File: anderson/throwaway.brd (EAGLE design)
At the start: 37.8 x 29.2 mm, 4 parts

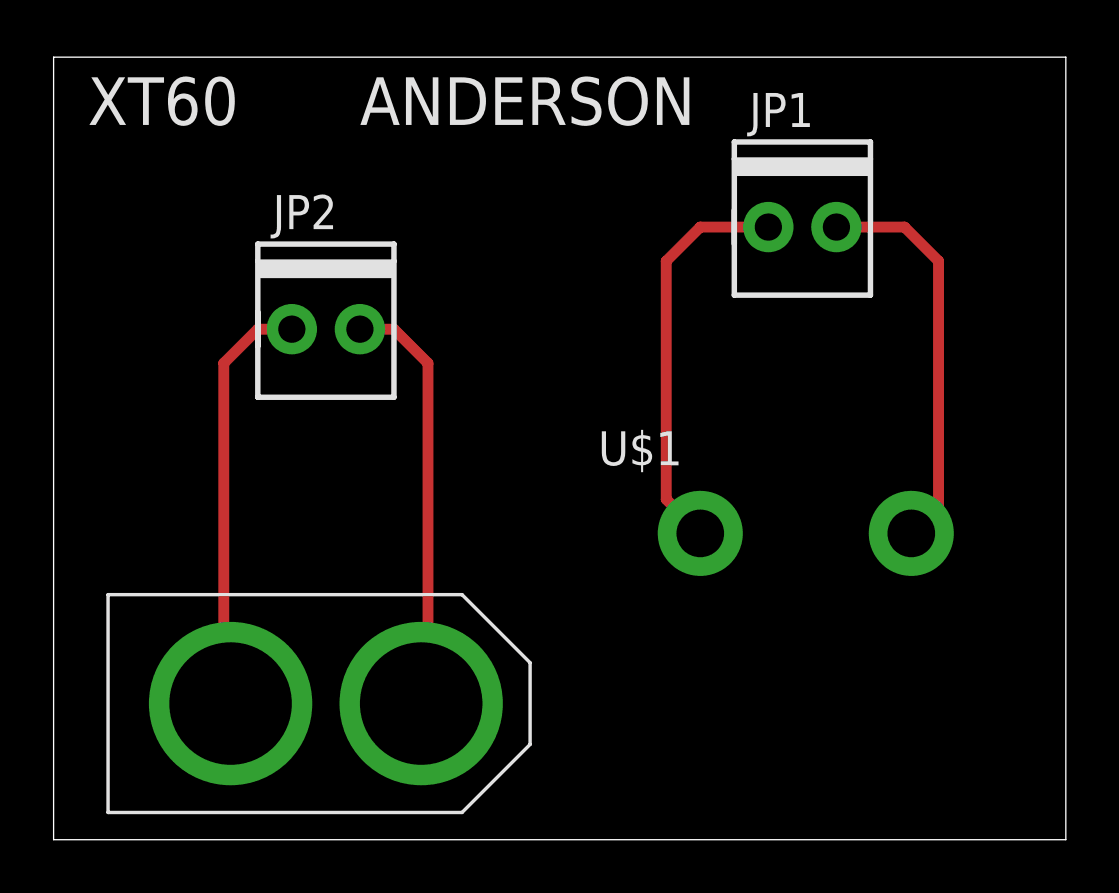
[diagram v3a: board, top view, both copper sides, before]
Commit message: Throwaway Board
XT60 Connectors and Anderson Connnectors  on throwaway
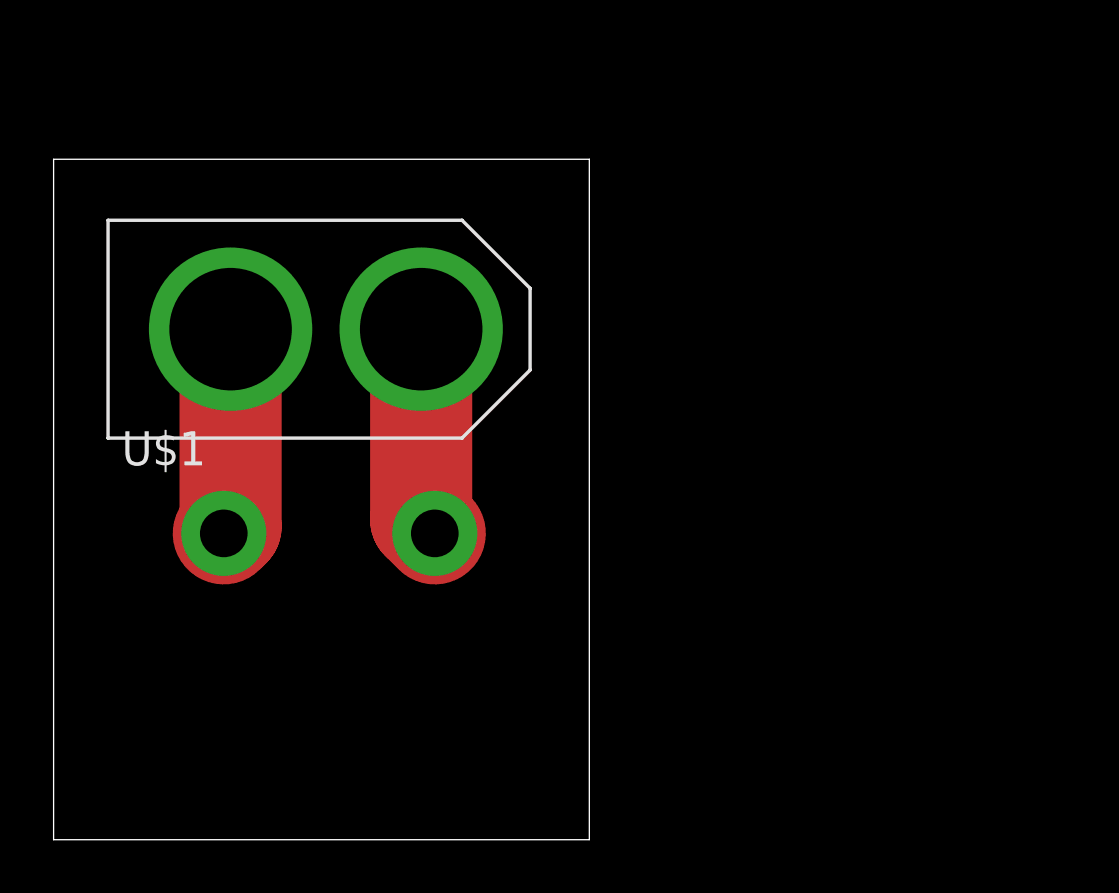
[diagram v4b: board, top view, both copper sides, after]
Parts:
- removed JP1, JP2: (no value), pie:1X02-MTA
- moved U$1 17.8 mm to (6.35, 11.4)
- moved U$3 14.0 mm to (10.2, 19.1)
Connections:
- removed net N$3: JP2.2, U$3.GND
- removed net N$4: JP2.1, U$3.12V
- net N$1: now also U$3.12V; no longer JP1.1
- net N$2: now also U$3.GND; no longer JP1.2
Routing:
- net N$3: track 15.9 -> 0.00 mm
- net N$4: track 15.9 -> 0.00 mm
- net N$1: track 15.0 -> 7.73 mm
- net N$2: track 14.9 -> 7.83 mm
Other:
- board size 37.8 x 29.2 mm -> 20 x 25.4 mm
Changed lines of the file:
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@@
 <layer number="20" name="Dimension" color="15" fill="1" visible="yes" active="yes"/>
 <layer number="21" name="tPlace" color="7" fill="1" visible="yes" active="yes"/>
-<layer number="22" name="bPlace" color="7" fill="1" visible="yes" active="yes"/>
+<layer number="22" name="bPlace" color="14" fill="1" visible="yes" active="yes"/>
 <layer number="23" name="tOrigins" color="15" fill="1" visible="yes" active="yes"/>
 <layer number="24" name="bOrigins" color="15" fill="1" visible="yes" active="yes"/>
 <layer number="25" name="tNames" color="7" fill="1" visible="yes" active="yes"/>
-<layer number="26" name="bNames" color="7" fill="1" visible="yes" active="yes"/>
+<layer number="26" name="bNames" color="14" fill="1" visible="yes" active="yes"/>
 <layer number="27" name="tValues" color="7" fill="1" visible="yes" active="yes"/>
 <layer number="28" name="bValues" color="7" fill="1" visible="yes" active="yes"/>
@@
 <board>
 <plain>
-<wire x1="0" y1="0" x2="37.77" y2="0" width="0" layer="20"/>
-<wire x1="37.77" y1="0" x2="37.77" y2="29.2" width="0" layer="20"/>
-<wire x1="37.77" y1="29.2" x2="0" y2="29.2" width="0" layer="20"/>
-<wire x1="0" y1="29.2" x2="0" y2="0" width="0" layer="20"/>
-<text x="1.27" y="26.67" size="1.778" layer="25" font="vector">XT60</text>
-<text x="11.43" y="26.67" size="1.778" layer="25" font="vector">ANDERSON</text>
+<wire x1="0" y1="0" x2="19.99" y2="0" width="0" layer="20"/>
+<wire x1="19.99" y1="0" x2="19.99" y2="25.39" width="0" layer="20"/>
+<wire x1="19.99" y1="25.39" x2="0" y2="25.39" width="0" layer="20"/>
+<wire x1="0" y1="25.39" x2="0" y2="0" width="0" layer="20"/>
+<text x="12.7" y="13.97" size="1.778" layer="26" font="vector" rot="MR0">XT60</text>
+<text x="16.51" y="7.62" size="1.778" layer="26" font="vector" rot="MR0">ANDERSON</text>
 </plain>
 <attributes>
@@
 </autorouter>
 <elements>
-<element name="JP1" library="pie" package="1X02-MTA" value="" x="27.94" y="22.86">
-<attribute name="PARTNUMBER" value="A1921-ND" x="60.96" y="13.97" size="1.778" layer="27" display="off"/>
+<element name="U$3" library="pie" package="XT60CONNECTOR" value="XT60CONNECTOR" x="10.16" y="19.05">
+<attribute name="PARTNUMBER" value="PRT-10474 " x="31.75" y="-25.4" size="1.778" layer="27" display="off"/>
 </element>
-<element name="U$3" library="pie" package="XT60CONNECTOR" value="XT60CONNECTOR" x="10.16" y="5.08">
-<attribute name="PARTNUMBER" value="PRT-10474 " x="31.75" y="-39.37" size="1.778" layer="27" display="off"/>
-</element>
-<element name="JP2" library="pie" package="1X02-MTA" value="" x="10.16" y="19.05">
-<attribute name="PARTNUMBER" value="A1921-ND" x="49.53" y="10.16" size="1.778" layer="27" display="off"/>
-</element>
-<element name="U$1" library="pie" package="ANDERSON_25A_1X2" value="ANDERSON_25A_1X2" x="24.13" y="11.43"/>
+<element name="U$1" library="pie" package="ANDERSON_25A_1X2" value="ANDERSON_25A_1X2" x="6.35" y="11.43"/>
 </elements>
 <signals>
-<signal name="N$3">
-<contactref element="U$3" pad="GND"/>
-<contactref element="JP2" pad="2"/>
-<wire x1="11.43" y1="19.05" x2="12.7" y2="19.05" width="0.4064" layer="1"/>
-<wire x1="12.7" y1="19.05" x2="13.97" y2="17.78" width="0.4064" layer="1"/>
-<wire x1="13.97" y1="17.78" x2="13.97" y2="5.334" width="0.4064" layer="1"/>
-<wire x1="13.97" y1="5.334" x2="13.716" y2="5.08" width="0.4064" layer="1"/>
-</signal>
-<signal name="N$4">
+<signal name="N$1">
 <contactref element="U$3" pad="12V"/>
-<contactref element="JP2" pad="1"/>
-<wire x1="8.89" y1="19.05" x2="7.62" y2="19.05" width="0.4064" layer="1"/>
-<wire x1="7.62" y1="19.05" x2="6.35" y2="17.78" width="0.4064" layer="1"/>
-<wire x1="6.35" y1="17.78" x2="6.35" y2="5.334" width="0.4064" layer="1"/>
-<wire x1="6.35" y1="5.334" x2="6.604" y2="5.08" width="0.4064" layer="1"/>
-</signal>
-<signal name="N$1">
 <contactref element="U$1" pad="PIN1"/>
-<contactref element="JP1" pad="1"/>
-<wire x1="26.67" y1="22.86" x2="24.13" y2="22.86" width="0.4064" layer="1"/>
-<wire x1="24.13" y1="22.86" x2="22.86" y2="21.59" width="0.4064" layer="1"/>
-<wire x1="22.86" y1="21.59" x2="22.86" y2="12.7" width="0.4064" layer="1"/>
-<wire x1="22.86" y1="12.7" x2="24.13" y2="11.43" width="0.4064" layer="1"/>
+<wire x1="6.604" y1="19.05" x2="6.604" y2="11.684" width="3.81" layer="1"/>
+<wire x1="6.604" y1="11.684" x2="6.35" y2="11.43" width="3.81" layer="1"/>
 </signal>
 <signal name="N$2">
+<contactref element="U$3" pad="GND"/>
 <contactref element="U$1" pad="PIN2"/>
-<contactref element="JP1" pad="2"/>
-<wire x1="29.21" y1="22.86" x2="31.75" y2="22.86" width="0.4064" layer="1"/>
-<wire x1="31.75" y1="22.86" x2="33.02" y2="21.59" width="0.4064" layer="1"/>
-<wire x1="33.02" y1="21.59" x2="33.02" y2="12.446" width="0.4064" layer="1"/>
-<wire x1="33.02" y1="12.446" x2="32.004" y2="11.43" width="0.4064" layer="1"/>
+<wire x1="13.716" y1="19.05" x2="13.716" y2="11.938" width="3.81" layer="1"/>
+<wire x1="13.716" y1="11.938" x2="14.224" y2="11.43" width="3.81" layer="1"/>
 </signal>
 </signals>

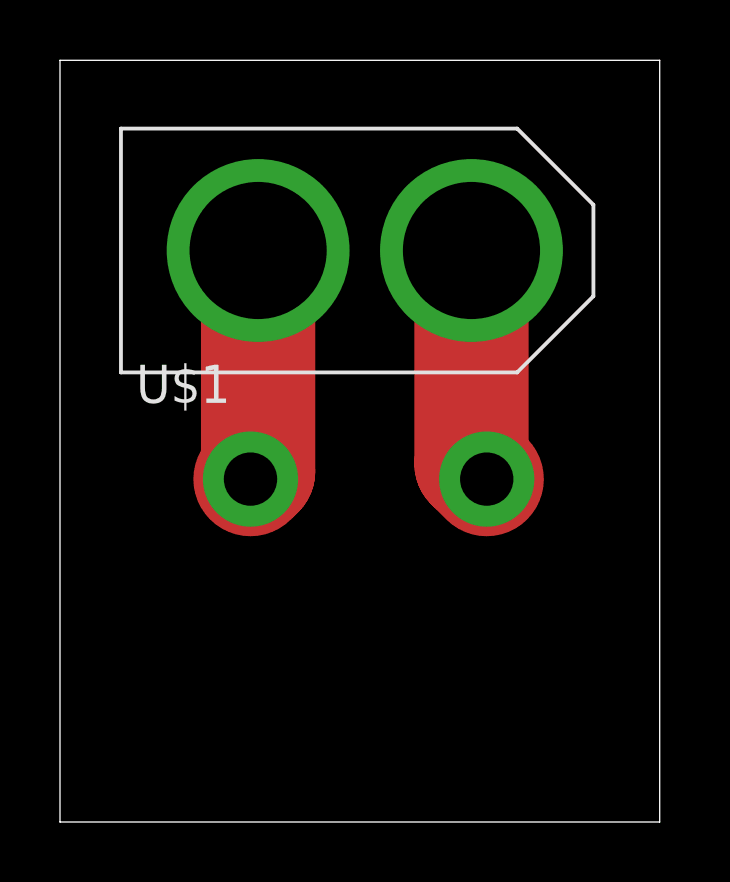
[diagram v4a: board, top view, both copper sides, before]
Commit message: Throwaway Board again...
removed traces used polygon instead.
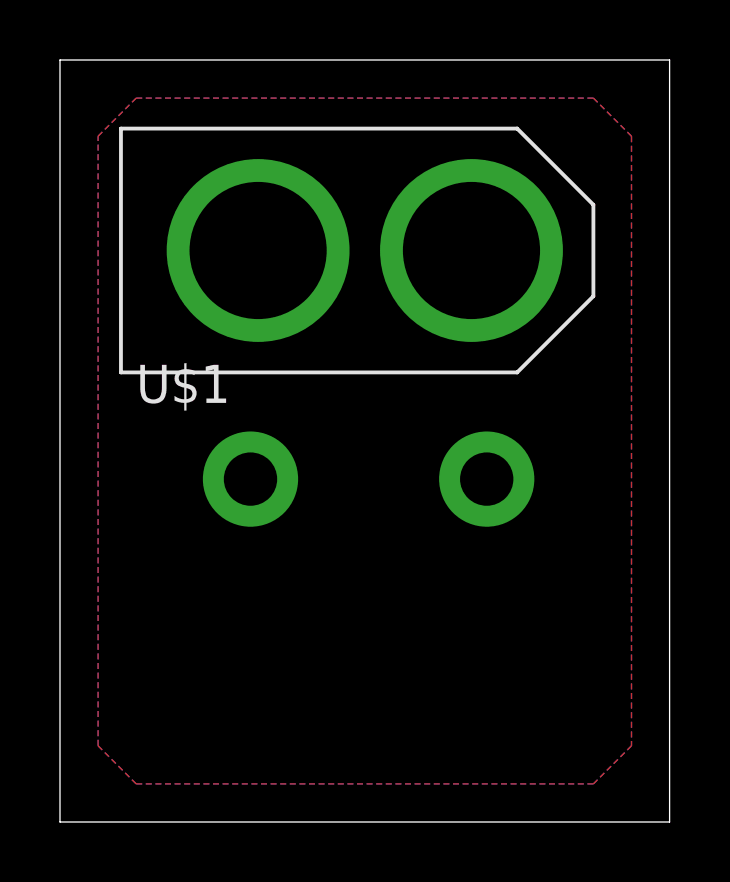
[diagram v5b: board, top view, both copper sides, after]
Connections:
- net N$1 renamed 1
- net N$2 renamed 2
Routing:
- net 2: track 7.83 -> 0.00 mm
- net 1: track 7.73 -> 0.00 mm
- added copper zone on layer 1, net 1
- added copper zone on layer 16, net 2
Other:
- board size 20 x 25.4 mm -> 20.3 x 25.4 mm
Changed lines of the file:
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@@
 <board>
 <plain>
-<wire x1="0" y1="0" x2="19.99" y2="0" width="0" layer="20"/>
-<wire x1="19.99" y1="0" x2="19.99" y2="25.39" width="0" layer="20"/>
-<wire x1="19.99" y1="25.39" x2="0" y2="25.39" width="0" layer="20"/>
-<wire x1="0" y1="25.39" x2="0" y2="0" width="0" layer="20"/>
+<wire x1="0" y1="0" x2="20.32" y2="0" width="0" layer="20"/>
+<wire x1="20.32" y1="0" x2="20.32" y2="25.4" width="0" layer="20"/>
+<wire x1="20.32" y1="25.4" x2="0" y2="25.4" width="0" layer="20"/>
+<wire x1="0" y1="25.4" x2="0" y2="0" width="0" layer="20"/>
 <text x="12.7" y="13.97" size="1.778" layer="26" font="vector" rot="MR0">XT60</text>
 <text x="16.51" y="7.62" size="1.778" layer="26" font="vector" rot="MR0">ANDERSON</text>
@@
 </elements>
 <signals>
-<signal name="N$1">
+<signal name="1">
 <contactref element="U$3" pad="12V"/>
 <contactref element="U$1" pad="PIN1"/>
-<wire x1="6.604" y1="19.05" x2="6.604" y2="11.684" width="3.81" layer="1"/>
-<wire x1="6.604" y1="11.684" x2="6.35" y2="11.43" width="3.81" layer="1"/>
+<polygon width="0.254" layer="1">
+<vertex x="2.54" y="24.13"/>
+<vertex x="17.78" y="24.13"/>
+<vertex x="19.05" y="22.86"/>
+<vertex x="19.05" y="2.54"/>
+<vertex x="17.78" y="1.27"/>
+<vertex x="2.54" y="1.27"/>
+<vertex x="1.27" y="2.54"/>
+<vertex x="1.27" y="22.86"/>
+</polygon>
 </signal>
-<signal name="N$2">
+<signal name="2">
 <contactref element="U$3" pad="GND"/>
 <contactref element="U$1" pad="PIN2"/>
-<wire x1="13.716" y1="19.05" x2="13.716" y2="11.938" width="3.81" layer="1"/>
-<wire x1="13.716" y1="11.938" x2="14.224" y2="11.43" width="3.81" layer="1"/>
+<polygon width="0.254" layer="16">
+<vertex x="2.54" y="24.13"/>
+<vertex x="17.78" y="24.13"/>
+<vertex x="19.05" y="22.86"/>
+<vertex x="19.05" y="2.54"/>
+<vertex x="17.78" y="1.27"/>
+<vertex x="2.54" y="1.27"/>
+<vertex x="1.27" y="2.54"/>
+<vertex x="1.27" y="22.86"/>
+</polygon>
 </signal>
 </signals>
